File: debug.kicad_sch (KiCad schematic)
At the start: 63 parts, among them J701 USB4105-GF-A, J702 Conn_02x10_Odd_Even, U701 USBLC6-2SC6, U702 FT231XQ-R, U703 TCA9554PW

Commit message: Update R & L BOM
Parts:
- R701, R702, R704, R710: Digi-Key Part Number (none) -> P10.0KLCT-ND; MPN (none) -> ERJ-2RKF1002X; Manufacturer (none) -> Panasonic Electronic Components
- R703, R705: Digi-Key Part Number (none) -> P5.10KLCT-ND; MPN (none) -> ERJ-2RKF5101X; Manufacturer (none) -> Panasonic Electronic Components
- R706, R707: Digi-Key Part Number (none) -> P33.0LCT-ND; MPN (none) -> ERJ-2RKF33R0X; Manufacturer (none) -> Panasonic Electronic Components
- R708, R709: Digi-Key Part Number (none) -> P4.70KLCT-ND; MPN (none) -> ERJ-2RKF4701X; Manufacturer (none) -> Panasonic Electronic Components
- R711, R712, R713, R718, R719, R720: footprint (none) -> perfect_footprints:R_0402_1005Metric; Digi-Key Part Number (none) -> P0.0JCT-ND; MPN (none) -> ERJ-2GE0R00X; Manufacturer (none) -> Panasonic Electronic Components
- R714, R715, R722, R723, R726, R727, R729, R730, R731, R732: Digi-Key Part Number (none) -> 732-560112110231CT-ND; MPN (none) -> 560112110231; Manufacturer (none) -> Würth Elektronik
- R716, R717, R721, R728: Digi-Key Part Number (none) -> P1.00KLCT-ND; MPN (none) -> ERJ-2RKF1001X; Manufacturer (none) -> Panasonic Electronic Components
- R724, R725: footprint (none) -> Resistor_SMD:R_0805_2012Metric; Digi-Key Part Number (none) -> P0.0ACT-ND; MPN (none) -> ERJ-6GEY0R00V; Manufacturer (none) -> Panasonic Electronic Components

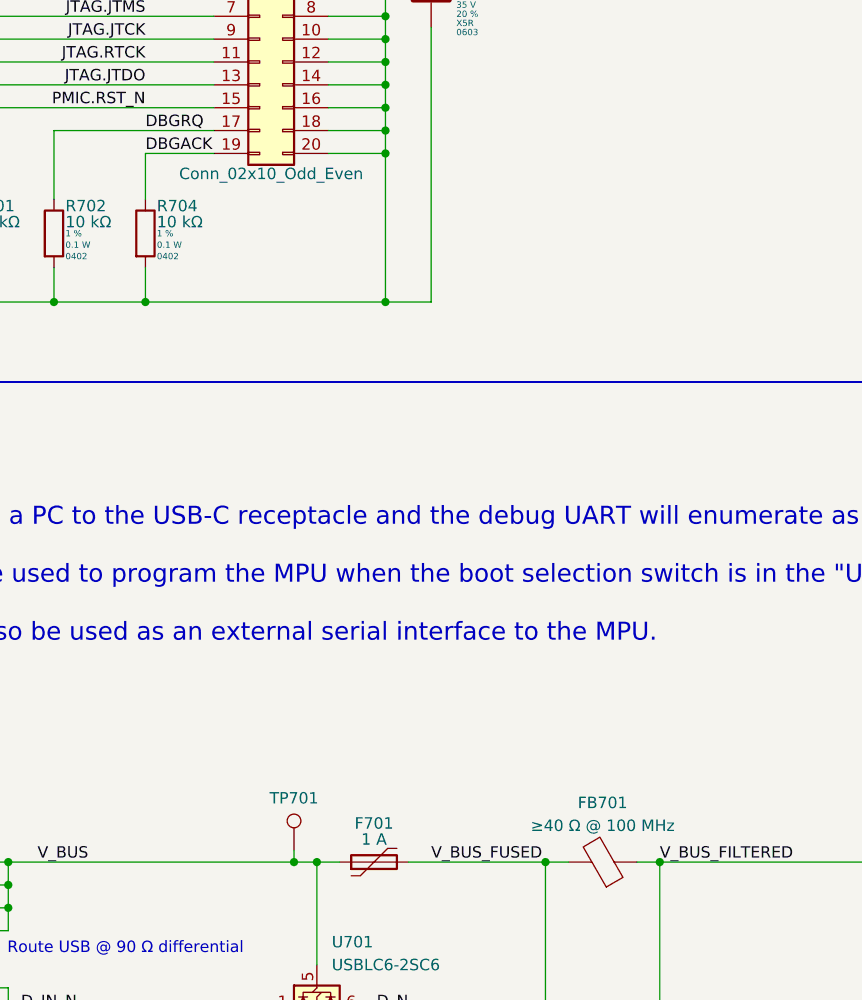
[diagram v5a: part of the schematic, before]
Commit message: Fill BOM info
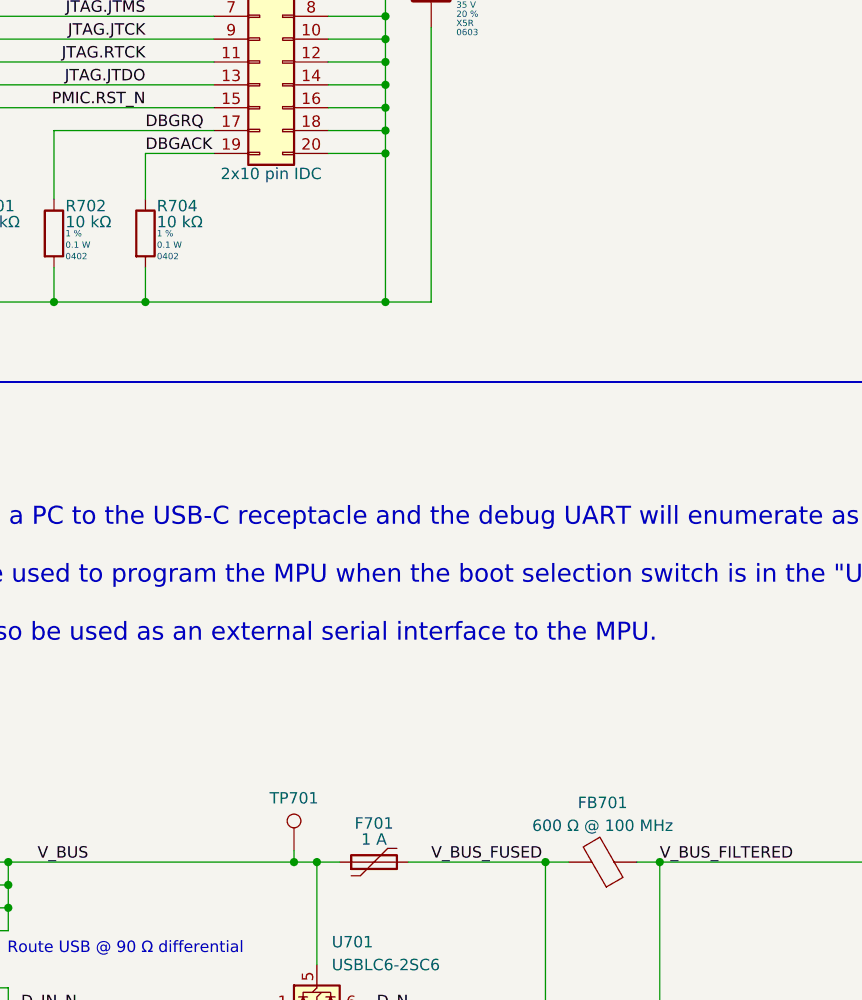
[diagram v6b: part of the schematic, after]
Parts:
- D701, D702, D703, D704: Digi-Key Part Number (none) -> 732-4978-1-ND
- F701: footprint (none) -> Fuse:Fuse_0805_2012Metric; Digi-Key Part Number (none) -> 5923-0ZCK0100FF2ECT-ND; MPN (none) -> 0ZCK0100FF2E; Manufacturer (none) -> Bel Fuse Inc.
- FB701: value ≥40 Ω @ 100 MHz -> 600 Ω @ 100 MHz; footprint (none) -> Inductor_SMD:L_0603_1608Metric; Digi-Key Part Number (none) -> 445-MPZ1608S601ATA00CT-ND; MPN (none) -> MPZ1608S601ATA00; Manufacturer (none) -> TDK Corporation
- J701: Digi-Key Part Number (none) -> 2073-USB4105-GF-ACT-ND
- J702: value Conn_02x10_Odd_Even -> 2x10 pin IDC; footprint Connector_IDC:IDC-Header_2x10_P2.54mm_Vertical_SMD -> Connector_IDC:IDC-Header_2x10_P2.54mm_Vertical; Digi-Key Part Number (none) -> S9172-ND; MPN (none) -> SBH11-PBPC-D10-ST-BK; Manufacturer (none) -> Sullins Connector Solutions
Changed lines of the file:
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@@
 			)
 		)
+		(property "Digi-Key Part Number" "732-4978-1-ND"
+			(at 260.35 193.04 90)
+			(effects
+				(font
+					(size 1.27 1.27)
+				)
+				(hide yes)
+			)
+		)
 		(pin "2"
 		)
@@
 			)
 		)
-		(property "Value" "≥40 Ω @ 100 MHz"
+		(property "Value" "600 Ω @ 100 MHz"
 			(at 120.65 187.198 90)
 			(effects
@@
 			)
 		)
-		(property "Footprint" ""
+		(property "Footprint" "Inductor_SMD:L_0603_1608Metric"
 			(at 120.65 192.278 90)
 			(effects
@@
 			)
 		)
-		(property "Datasheet" "~"
+		(property "Datasheet" "https://product.tdk.com/en/system/files?file=dam/doc/product/emc/emc/beads/catalog/beads_commercial_power_mpz1608_en.pdf"
 			(at 120.65 190.5 0)
 			(effects
@@
 			)
 		)
-		(property "Description" "Ferrite bead"
+		(property "Description" "600 Ohms @ 100 MHz 1 Power Line Ferrite Bead 0603 (1608 Metric) 1A 150mOhm"
 			(at 120.65 190.5 0)
 			(effects
@@
 			)
 		)
+		(property "Digi-Key Part Number" "445-MPZ1608S601ATA00CT-ND"
+			(at 120.65 190.5 90)
+			(effects
+				(font
+					(size 1.27 1.27)
+				)
+				(hide yes)
+			)
+		)
+		(property "MPN" "MPZ1608S601ATA00"
+			(at 120.65 190.5 90)
+			(effects
+				(font
+					(size 1.27 1.27)
+				)
+				(hide yes)
+			)
+		)
+		(property "Manufacturer" "TDK Corporation"
+			(at 120.65 190.5 90)
+			(effects
+				(font
+					(size 1.27 1.27)
+				)
+				(hide yes)
+			)
+		)
 		(pin "2"
 		)
@@
 			)
 		)
-		(property "Value" "Conn_02x10_Odd_Even"
+		(property "Value" "2x10 pin IDC"
 			(at 83.82 113.284 0)
 			(effects
@@
 			)
 		)
-		(property "Footprint" "Connector_IDC:IDC-Header_2x10_P2.54mm_Vertical_SMD"
+		(property "Footprint" "Connector_IDC:IDC-Header_2x10_P2.54mm_Vertical"
 			(at 82.55 99.06 0)
 			(effects
@@
 			)
 		)
-		(property "Datasheet" "~"
+		(property "Datasheet" "https://s3.amazonaws.com/catalogspreads-pdf/PAGE122%20.100%20SBH11%20SERIES%20MALE%20BOX%20HDR%20ST%20RA%20SMT.pdf"
+			(at 82.55 99.06 0)
+			(effects
+				(font
+					(size 1.27 1.27)
+				)
+				(hide yes)
+			)
+		)
+		(property "Description" "Connector Header Through Hole 20 position 0.100\" (2.54mm)"
+			(at 82.55 99.06 0)
+			(effects
+				(font
+					(size 1.27 1.27)
+				)
+				(hide yes)
+			)
+		)
+		(property "Digi-Key Part Number" "S9172-ND"
 			(at 82.55 99.06 0)
 			(effects
@@
 			)
 		)
-		(property "Description" "Generic connector, double row, 02x10, odd/even pin numbering scheme (row 1 odd numbers, row 2 even numbers), script generated (kicad-library-utils/schlib/autogen/connector/)"
+		(property "MPN" "SBH11-PBPC-D10-ST-BK"
+			(at 82.55 99.06 0)
+			(effects
+				(font
+					(size 1.27 1.27)
+				)
+				(hide yes)
+			)
+		)
+		(property "Manufacturer" "Sullins Connector Solutions"
 			(at 82.55 99.06 0)
 			(effects
@@
 			)
 		)
+		(property "Digi-Key Part Number" "732-4978-1-ND"
+			(at 266.7 81.28 90)
+			(effects
+				(font
+					(size 1.27 1.27)
+				)
+				(hide yes)
+			)
+		)
 		(pin "2"
 		)
@@
 			)
 		)
-		(property "Footprint" ""
+		(property "Footprint" "Fuse:Fuse_0805_2012Metric"
 			(at 100.33 189.23 0)
 			(effects
@@
 			)
 		)
-		(property "Datasheet" ""
+		(property "Datasheet" "https://belfuse.com/media/datasheets/products/circuit-protection/ds-cp-0zck-series.pdf"
 			(at 95.25 190.5 0)
 			(effects
@@
 			)
 		)
-		(property "Description" ""
+		(property "Description" "Polymeric PTC Resettable Fuse 6V 1 A Ih Surface Mount 0805 (2012 Metric), Concave"
 			(at 95.25 190.5 0)
 			(effects
@@
 			)
 		)
-		(property "Manufacturer" ""
+		(property "Manufacturer" "Bel Fuse Inc."
+			(at 95.25 190.5 90)
+			(effects
+				(font
+					(size 1.27 1.27)
+				)
+				(hide yes)
+			)
+		)
+		(property "MPN" "0ZCK0100FF2E"
 			(at 95.25 190.5 90)
 			(effects
@@
 			)
 		)
-		(property "MPN" ""
+		(property "Digi-Key Part Number" "5923-0ZCK0100FF2ECT-ND"
 			(at 95.25 190.5 90)
 			(effects
@@
 			)
 		)
+		(property "Digi-Key Part Number" "732-4978-1-ND"
+			(at 256.54 193.04 90)
+			(effects
+				(font
+					(size 1.27 1.27)
+				)
+				(hide yes)
+			)
+		)
 		(pin "2"
 		)
@@
 			)
 		)
+		(property "Digi-Key Part Number" "2073-USB4105-GF-ACT-ND"
+			(at 38.1 213.36 0)
+			(effects
+				(font
+					(size 1.27 1.27)
+				)
+				(hide yes)
+			)
+		)
 		(pin "S1"
 		)
@@
 			(effects
 				(font
+					(size 1.27 1.27)
+				)
+				(hide yes)
+			)
+		)
+		(property "Digi-Key Part Number" "732-4978-1-ND"
+			(at 270.51 81.28 90)
+			(effects
+				(font

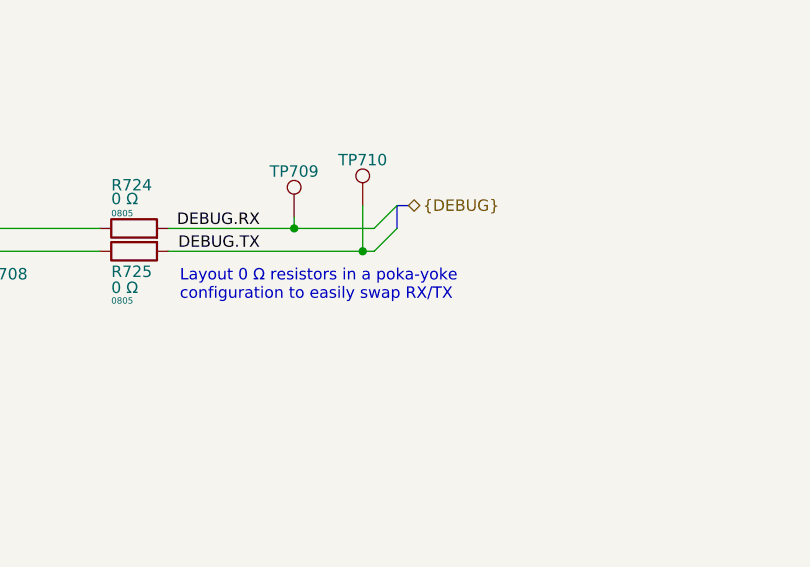
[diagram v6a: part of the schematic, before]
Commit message: Fill BOM information for the rest
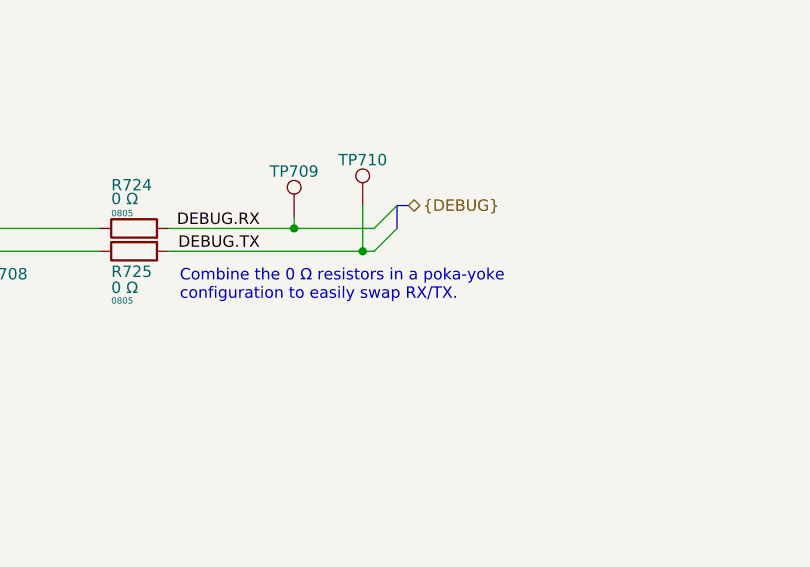
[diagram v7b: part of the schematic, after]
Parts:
- U701: Digi-Key Part Number (none) -> 497-5235-1-ND; MPN (none) -> USBLC6-2SC6; Manufacturer (none) -> STMicroelectronics
- U703: Digi-Key Part Number (none) -> 296-30135-1-ND; MPN (none) -> TCA9554PWR; Manufacturer (none) -> Texas Instruments
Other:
- note added: "Combine the 0 Ω resistors in a poka-yoke configuration to easily swap RX/TX."
- note removed: "Layout 0 Ω resistors in a poka-yoke configuration to easily swap RX/TX"
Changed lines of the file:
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@@
 		(rev "v0.0.1")
 	)
-	(text "Layout 0 Ω resistors in a poka-yoke\nconfiguration to easily swap RX/TX"
+	(text "Combine the 0 Ω resistors in a poka-yoke\nconfiguration to easily swap RX/TX."
 		(exclude_from_sim no)
 		(at 309.88 205.74 0)
@@
 			)
 		)
-		(property "Description" "8 Bit Port/Expander, I2C SMBUS, Interrupt output, TSSOP-16"
+		(property "Description" "I/O Expander 8 I2C, SMBus 400 kHz 16-TSSOP"
+			(at 241.3 115.57 0)
+			(effects
+				(font
+					(size 1.27 1.27)
+				)
+				(hide yes)
+			)
+		)
+		(property "Digi-Key Part Number" "296-30135-1-ND"
+			(at 241.3 115.57 0)
+			(effects
+				(font
+					(size 1.27 1.27)
+				)
+				(hide yes)
+			)
+		)
+		(property "MPN" "TCA9554PWR"
+			(at 241.3 115.57 0)
+			(effects
+				(font
+					(size 1.27 1.27)
+				)
+				(hide yes)
+			)
+		)
+		(property "Manufacturer" "Texas Instruments"
 			(at 241.3 115.57 0)
 			(effects
@@
 			)
 		)
-		(property "Datasheet" "https://www.st.com/resource/en/datasheet/usblc6-2.pdf"
+		(property "Datasheet" "https://www.st.com/resource/en/datasheet/cd00050750.pdf"
 			(at 90.17 215.265 0)
 			(effects
@@
 			)
 		)
-		(property "Description" "Very low capacitance ESD protection diode, 2 data-line, SOT-23-6"
+		(property "Description" "17V Clamp 5A (8/20µs) Ipp Tvs Diode Surface Mount SOT-23-6"
+			(at 88.9 207.01 0)
+			(effects
+				(font
+					(size 1.27 1.27)
+				)
+				(hide yes)
+			)
+		)
+		(property "Digi-Key Part Number" "497-5235-1-ND"
+			(at 88.9 207.01 0)
+			(effects
+				(font
+					(size 1.27 1.27)
+				)
+				(hide yes)
+			)
+		)
+		(property "MPN" "USBLC6-2SC6"
+			(at 88.9 207.01 0)
+			(effects
+				(font
+					(size 1.27 1.27)
+				)
+				(hide yes)
+			)
+		)
+		(property "Manufacturer" "STMicroelectronics"
 			(at 88.9 207.01 0)
 			(effects

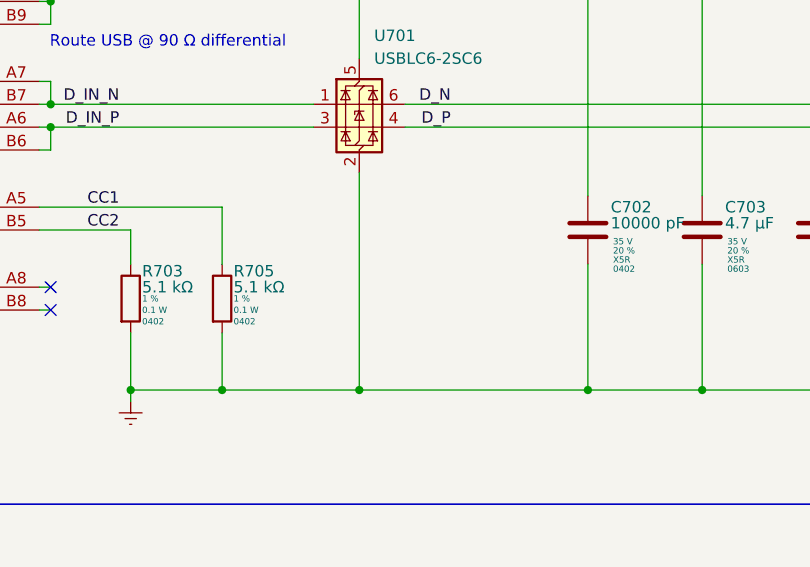
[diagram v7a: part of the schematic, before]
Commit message: Connect ESD TVS to chassis where possible, update version and date
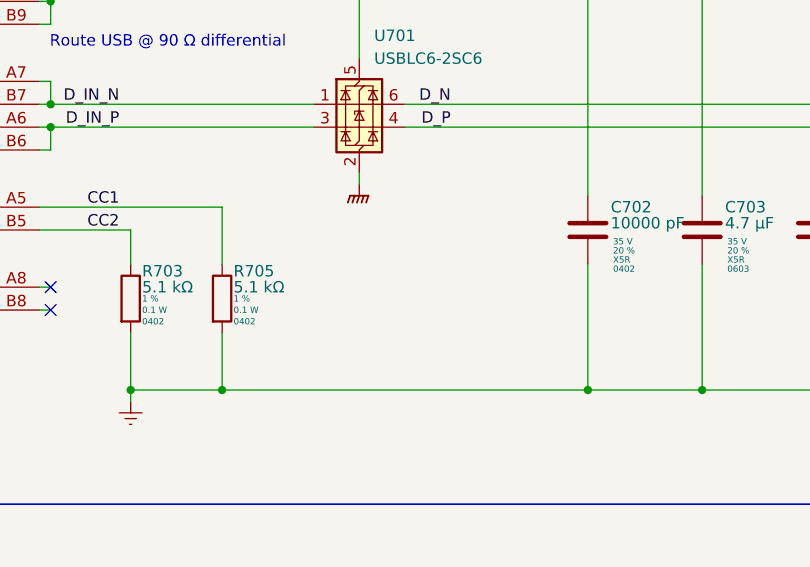
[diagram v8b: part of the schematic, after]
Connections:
- net CHASSIS: now also U701.2 (GND)
- net GND: no longer U701.2 (GND)
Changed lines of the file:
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@@
 	(title_block
 		(title "Linux SBC")
-		(date "2025-11-07")
-		(rev "v0.0.1")
+		(date "2025-12-14")
+		(rev "v1.0.0")
 	)
 	(text "Combine the 0 Ω resistors in a poka-yoke\nconfiguration to easily swap RX/TX."
@@
 	)
 	(junction
-		(at 88.9 238.76)
-		(diameter 0)
-		(color 0 0 0 0)
-	)
-	(junction
 		(at 298.45 72.39)
 		(diameter 0)
@@
 	(wire
 		(pts
-			(xy 73.66 238.76) (xy 88.9 238.76)
-		)
-		(stroke
-			(width 0)
-			(type default)
-		)
-	)
-	(wire
-		(pts
 			(xy 266.7 90.17) (xy 266.7 85.09)
 		)
@@
 	(wire
 		(pts
+			(xy 88.9 214.63) (xy 88.9 215.9)
+		)
+		(stroke
+			(width 0)
+			(type default)
+		)
+	)
+	(wire
+		(pts
 			(xy 266.7 107.95) (xy 266.7 97.79)
 		)
@@
 	(wire
 		(pts
-			(xy 88.9 214.63) (xy 88.9 238.76)
-		)
-		(stroke
-			(width 0)
-			(type default)
-		)
-	)
-	(wire
-		(pts
 			(xy 270.51 207.01) (xy 273.05 207.01)
 		)
@@
 	(wire
 		(pts
-			(xy 88.9 238.76) (xy 114.3 238.76)
+			(xy 73.66 238.76) (xy 114.3 238.76)
 		)
 		(stroke
@@
 		(dnp no)
 		(fields_autoplaced yes)
-		(property "Reference" "#PWR0706"
+		(property "Reference" "#PWR0707"
 			(at 241.3 139.7 0)
 			(effects
@@
 			(project "linux-sbc"
 				(path "/fa11a02f-8043-4153-ab69-88d766503017/5e32b227-0684-45b9-8c92-9550e4036164"
-					(reference "#PWR0706")
+					(reference "#PWR0707")
 					(unit 1)
 				)
@@
 	)
 	(symbol
+		(lib_id "power:GNDPWR")
+		(at 88.9 215.9 0)
+		(unit 1)
+		(exclude_from_sim no)
+		(in_bom yes)
+		(on_board yes)
+		(dnp no)
+		(fields_autoplaced yes)
+		(property "Reference" "#PWR0705"
+			(at 88.9 220.98 0)
+			(effects
+				(font
+					(size 1.27 1.27)
+				)
+				(hide yes)
+			)
+		)
+		(property "Value" "CHASSIS"
+			(at 88.773 219.71 0)
+			(effects
+				(font
+					(size 1.27 1.27)
+				)
+				(hide yes)
+			)
+		)
+		(property "Footprint" ""
+			(at 88.9 217.17 0)
+			(effects
+				(font
+					(size 1.27 1.27)
+				)
+				(hide yes)
+			)
+		)
+		(property "Datasheet" ""
+			(at 88.9 217.17 0)
+			(effects
+				(font
+					(size 1.27 1.27)
+				)
+				(hide yes)
+			)
+		)
+		(property "Description" "Power symbol creates a global label with name \"GNDPWR\" , global ground"
+			(at 88.9 215.9 0)
+			(effects
+				(font
+					(size 1.27 1.27)
+				)
+				(hide yes)
+			)
+		)
+		(pin "1"
+		)
+		(instances
+			(project "linux-sbc"
+				(path "/fa11a02f-8043-4153-ab69-88d766503017/5e32b227-0684-45b9-8c92-9550e4036164"
+					(reference "#PWR0705")
+					(unit 1)
+				)
+			)
+		)
+	)
+	(symbol
 		(lib_name "R_1")
 		(lib_id "Device:R")
@@
 		(dnp no)
 		(fields_autoplaced yes)
-		(property "Reference" "#PWR0705"
+		(property "Reference" "#PWR0706"
 			(at 234.95 105.41 0)
 			(effects
@@
 			(project "linux-sbc"
 				(path "/fa11a02f-8043-4153-ab69-88d766503017/5e32b227-0684-45b9-8c92-9550e4036164"
-					(reference "#PWR0705")
+					(reference "#PWR0706")
 					(unit 1)
 				)
@@
 		(on_board yes)
 		(dnp no)
-		(property "Reference" "#PWR0707"
+		(property "Reference" "#PWR0708"
 			(at 266.7 74.93 0)
 			(effects
@@
 			(project "linux-sbc"
 				(path "/fa11a02f-8043-4153-ab69-88d766503017/5e32b227-0684-45b9-8c92-9550e4036164"
-					(reference "#PWR0707")
+					(reference "#PWR0708")
 					(unit 1)
 				)
